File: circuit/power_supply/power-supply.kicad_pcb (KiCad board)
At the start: 2 copper layers, 21 parts, among them P1 CONN_2, U1 MCS34063A

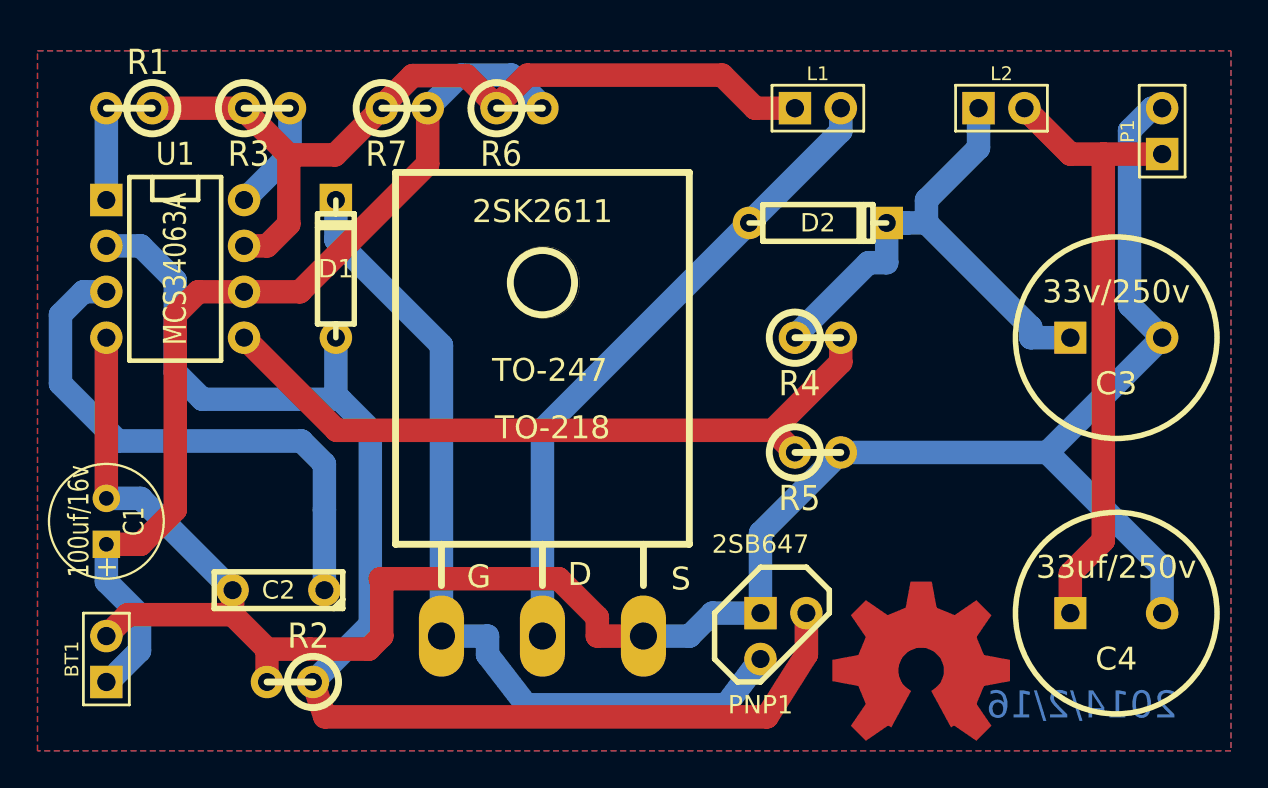
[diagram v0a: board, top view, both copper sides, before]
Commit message: Power supply board: Add the board edge
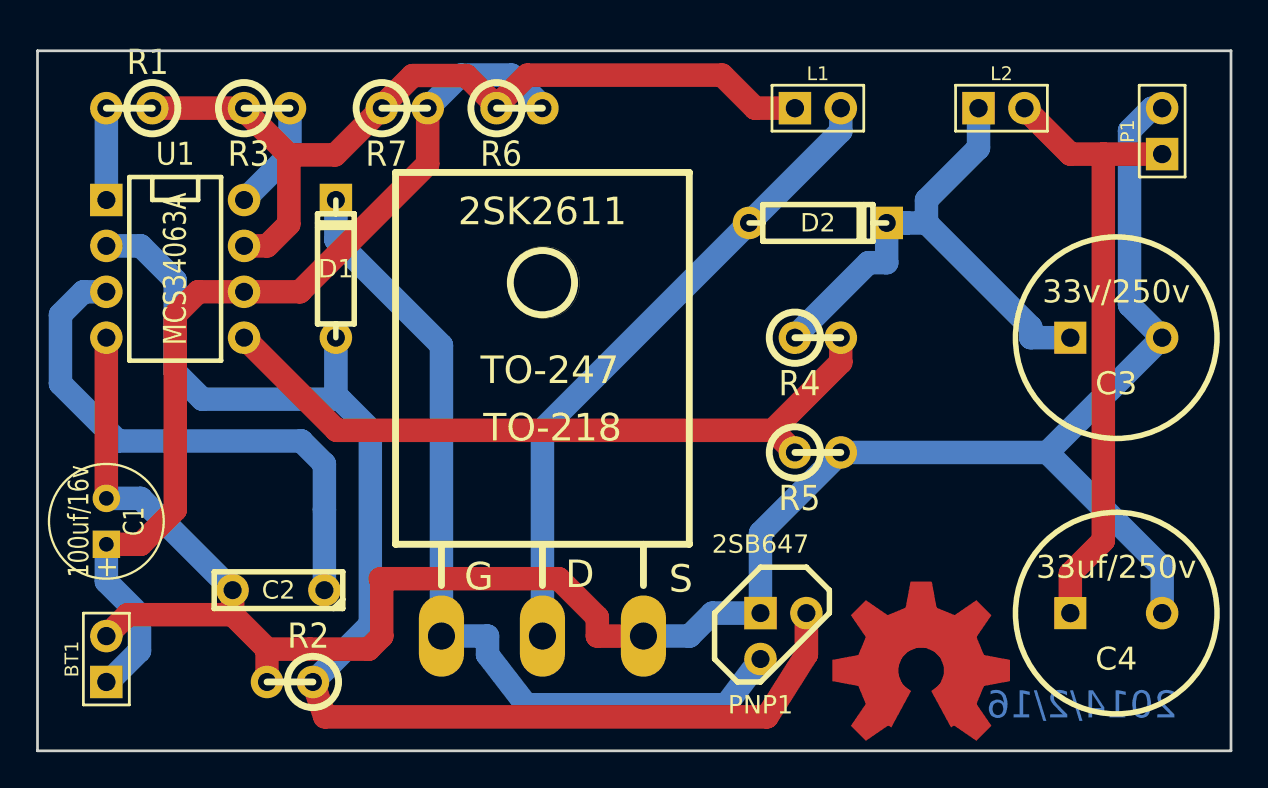
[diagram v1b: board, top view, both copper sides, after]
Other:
- board outline added: 66 x 38.7 mm
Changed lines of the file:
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@@
-(kicad_pcb (version 3) (host pcbnew "(2013-mar-13)-testing")
+(kicad_pcb (version 3) (host pcbnew "(2013-jul-07)-stable")
   (general
     (links 36)
     (no_connects 0)
-    (area 115.57 89.1159 181.991 130.7084)
+    (area 115.494999 89.1159 181.991 130.7084)
     (thickness 1.6)
-    (drawings 1)
+    (drawings 5)
     (tracks 126)
     (zones 0)
@@
     (tags "Transistor FET GDS TO-247 TO-218 TOP-3")
     (fp_text reference 2SK2611 (at 0 -23.495) (layer F.SilkS)
-      (effects (font (thickness 0.3048)))
+      (effects (font (size 1.524 1.524) (thickness 0.3048)))
     )
     (fp_text value MOSFET-N (at -1.27 5.08) (layer F.SilkS) hide
-      (effects (font (thickness 0.3048)))
+      (effects (font (size 1.524 1.524) (thickness 0.3048)))
     )
     (fp_line (start -5.588 -2.794) (end -5.588 -5.08) (layer F.SilkS) (width 0.381))
@@
     (fp_line (start 5.588 -2.794) (end 5.588 -5.08) (layer F.SilkS) (width 0.381))
     (fp_text user TO-218 (at 0.5588 -11.5316) (layer F.SilkS)
-      (effects (font (thickness 0.3048)))
+      (effects (font (size 1.524 1.524) (thickness 0.3048)))
     )
     (fp_text user TO-247 (at 0.4064 -14.7066) (layer F.SilkS)
-      (effects (font (thickness 0.3048)))
+      (effects (font (size 1.524 1.524) (thickness 0.3048)))
     )
     (fp_circle (center 0 -19.558) (end 1.778 -19.558) (layer F.SilkS) (width 0.381))
     (fp_text user S (at 7.6581 -3.1623) (layer F.SilkS)
-      (effects (font (thickness 0.3048)))
+      (effects (font (size 1.524 1.524) (thickness 0.3048)))
     )
     (fp_text user D (at 2.0701 -3.4163) (layer F.SilkS)
-      (effects (font (thickness 0.3048)))
+      (effects (font (size 1.524 1.524) (thickness 0.3048)))
     )
     (fp_text user G (at -3.5179 -3.2893) (layer F.SilkS)
-      (effects (font (thickness 0.3048)))
+      (effects (font (size 1.524 1.524) (thickness 0.3048)))
     )
     (fp_line (start 8.128 -25.654) (end 8.128 -5.08) (layer F.SilkS) (width 0.381))
@@
     (at 164.465 123.825)
     (fp_text reference OSHW_COPPER_10MM (at 0.635 5.715) (layer F.SilkS) hide
-      (effects (font (thickness 0.3048)))
+      (effects (font (size 1.524 1.524) (thickness 0.3048)))
     )
     (fp_text value VAL** (at 0 0) (layer F.SilkS) hide
-      (effects (font (thickness 0.3048)))
+      (effects (font (size 1.524 1.524) (thickness 0.3048)))
     )
     (pad "" smd trapezoid (at 0 -4.1656 180) (size 1.45796 1.4986) (rect_delta 0 -0.2794 )
@@
     )
   )
+  (gr_line (start 115.57 128.27) (end 181.61 128.27) (angle 90) (layer Edge.Cuts) (width 0.15))
+  (gr_line (start 115.57 89.535) (end 115.57 128.27) (angle 90) (layer Edge.Cuts) (width 0.15))
+  (gr_line (start 181.61 89.535) (end 115.57 89.535) (angle 90) (layer Edge.Cuts) (width 0.15))
+  (gr_line (start 181.61 128.27) (end 181.61 89.535) (angle 90) (layer Edge.Cuts) (width 0.15))
   (gr_text 2014/2/16 (at 173.355 125.73) (layer B.Cu)
     (effects (font (size 1.5 1.5) (thickness 0.35)) (justify mirror))

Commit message: Remove the coper zone
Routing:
- removed copper zone on B.Cu, net (none)
- removed copper zone on F.Cu, net (none)

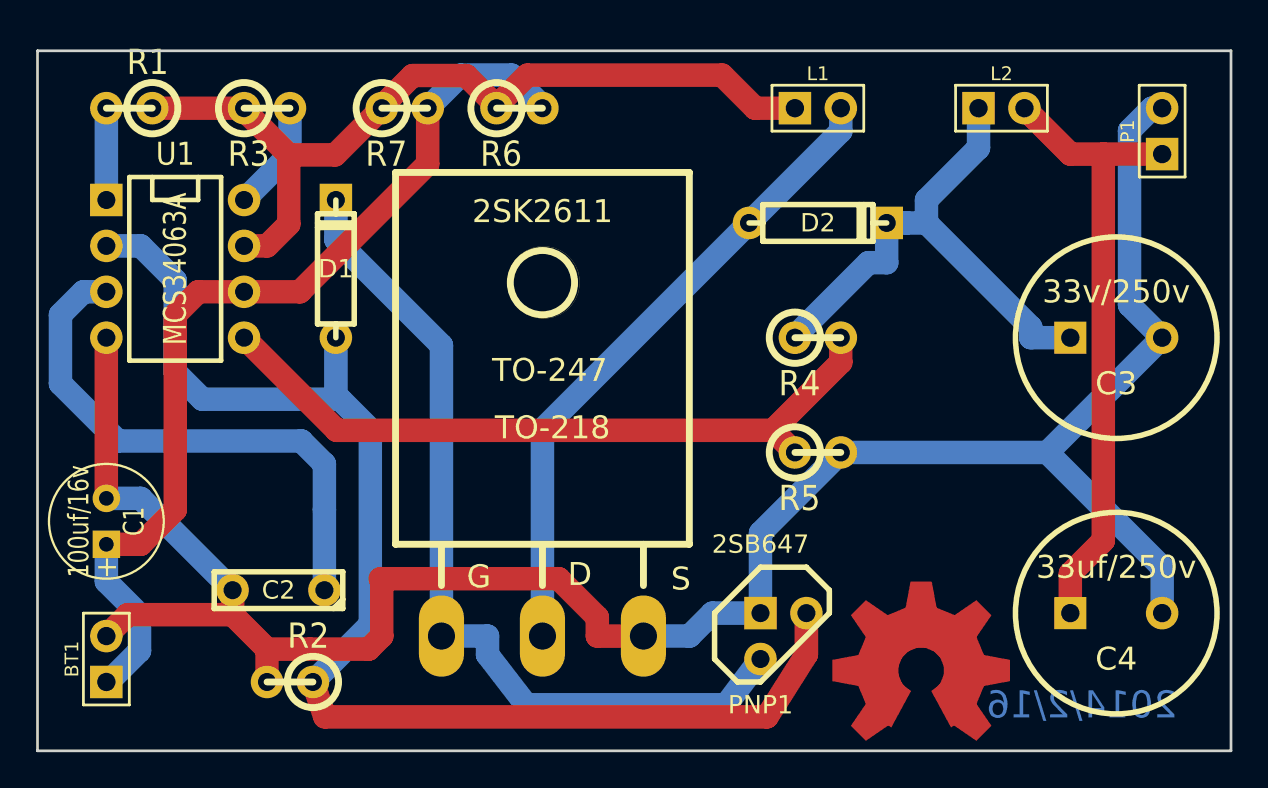
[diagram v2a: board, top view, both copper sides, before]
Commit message: Power supply board: Arrange the label
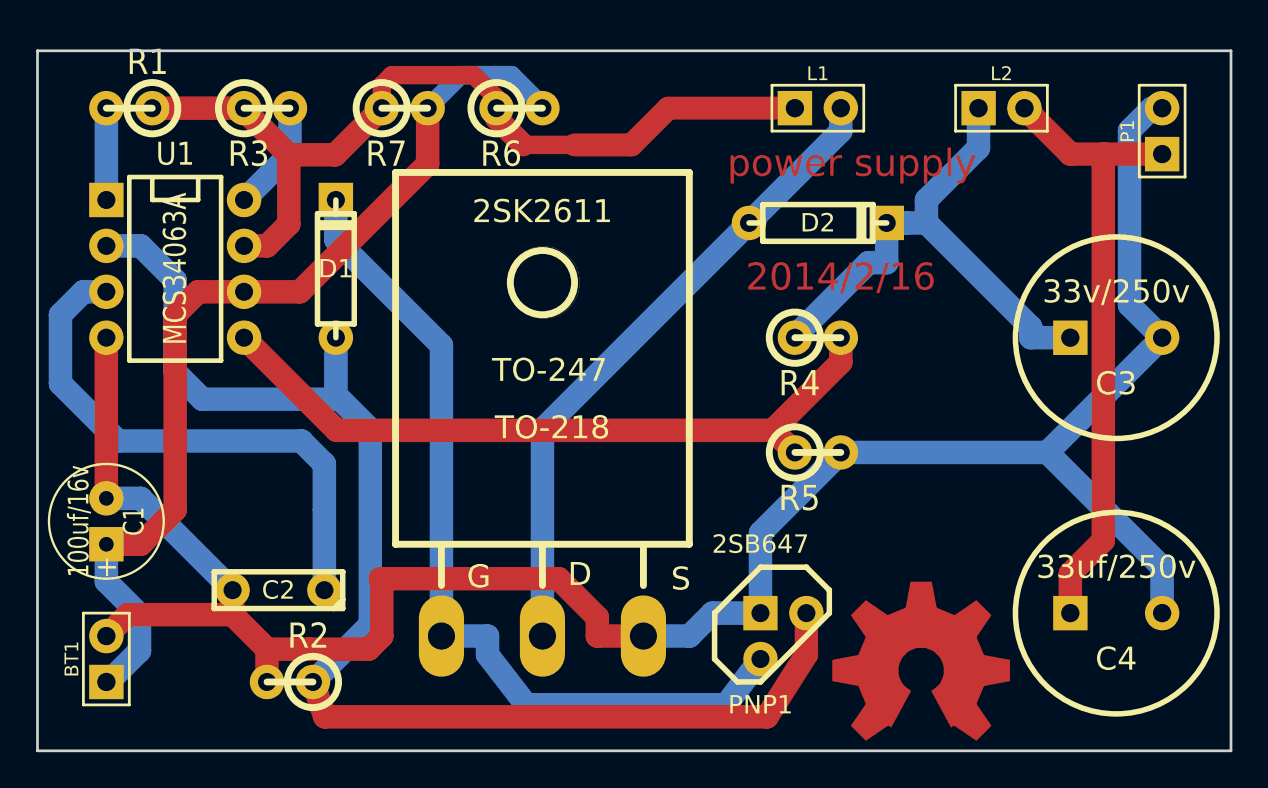
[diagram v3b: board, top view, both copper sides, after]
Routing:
- net N-000009: track 47.7 -> 57.5 mm
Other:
- board text added: "power supply"

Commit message: Power supply board: Arrange the track line
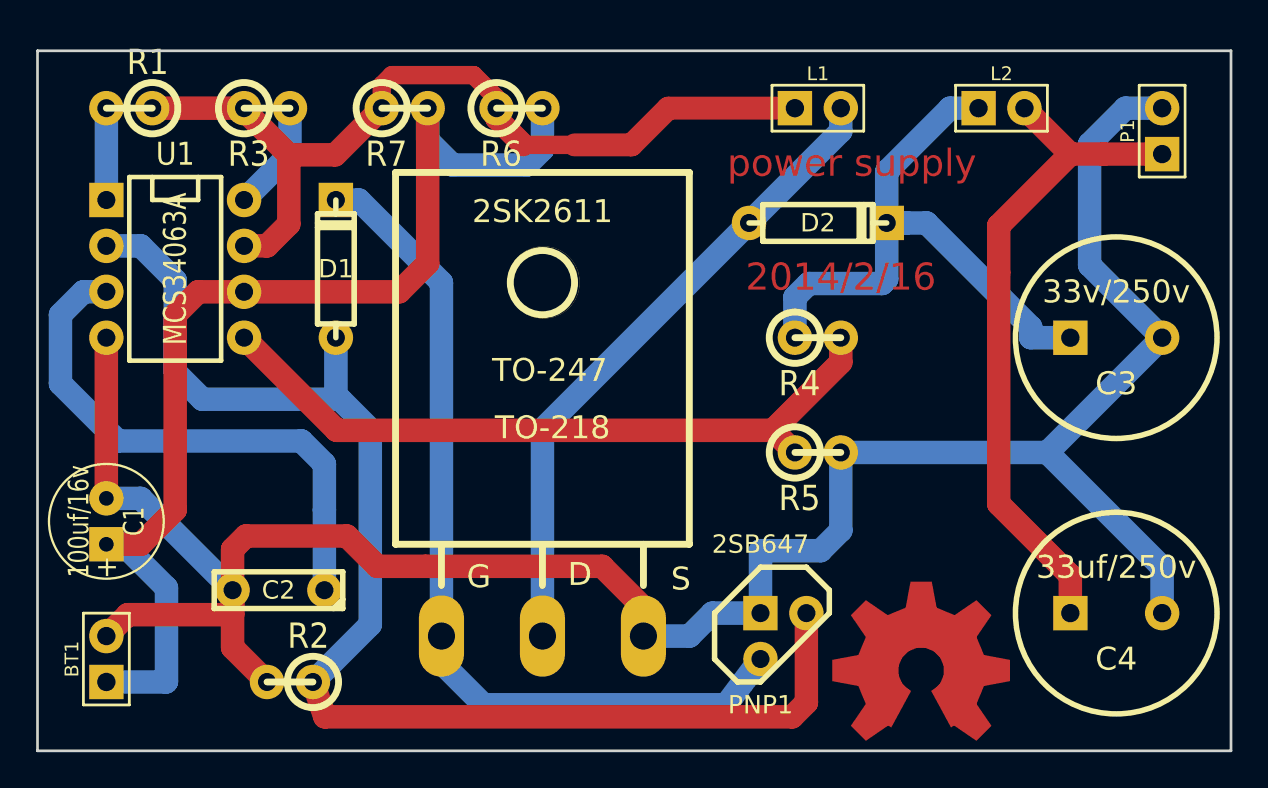
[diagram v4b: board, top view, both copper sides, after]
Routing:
- net N-0000011: track 53.2 -> 64.0 mm
- net N-000001: track 121.8 -> 130.6 mm
- net N-000003: track 29.7 -> 33.4 mm
- net N-000006: track 34.8 -> 37.4 mm
- net N-000008: track 73.4 -> 74.4 mm
- net N-000005: track 47.9 -> 48.7 mm

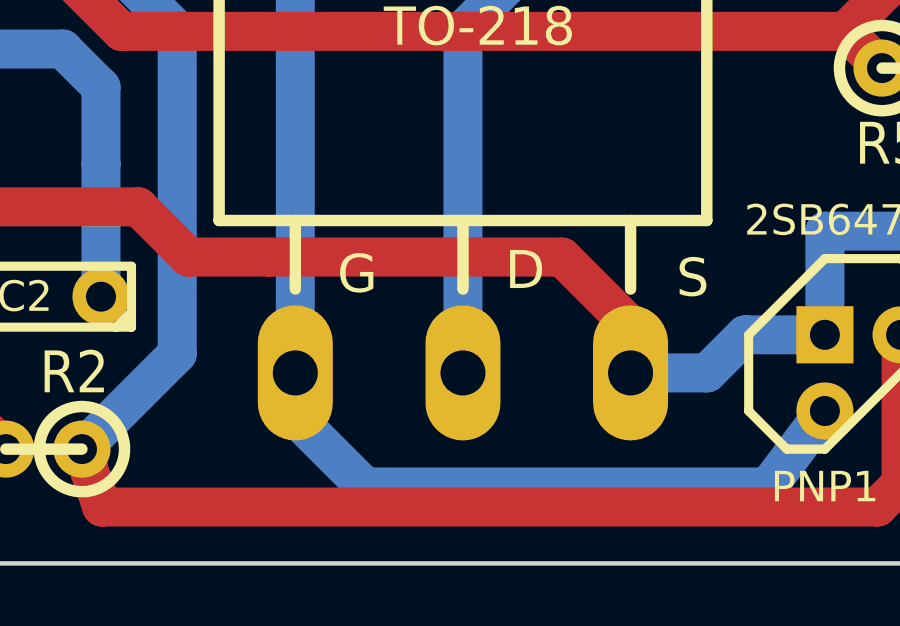
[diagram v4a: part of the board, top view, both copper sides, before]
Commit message: Control board: Optimize some auto-route layout
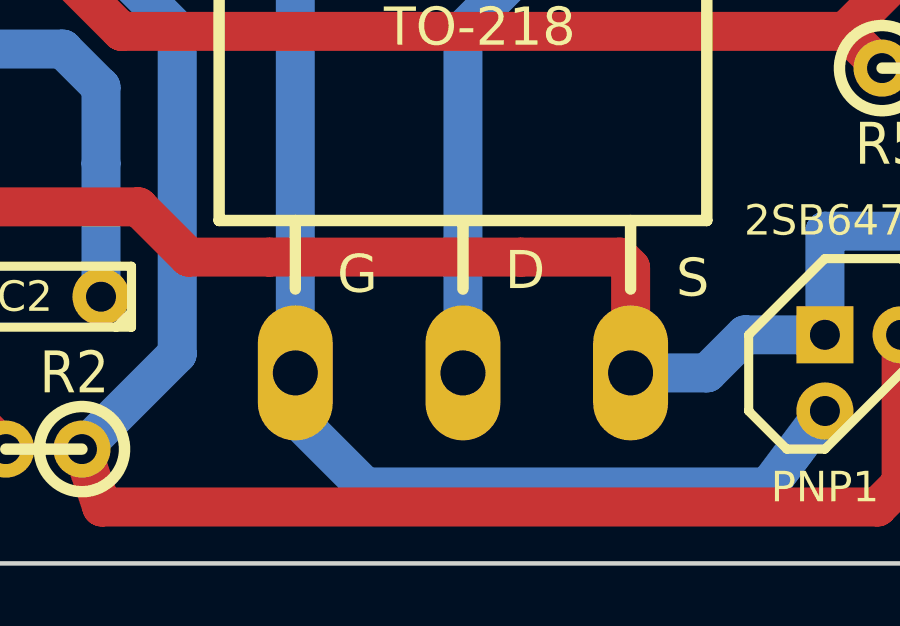
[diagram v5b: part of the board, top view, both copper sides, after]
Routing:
- net N-000001: track 130.6 -> 133.3 mm
